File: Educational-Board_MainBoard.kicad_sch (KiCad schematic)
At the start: 0 parts

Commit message: Aggiunto nomi
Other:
- company: (none) -> Filippo Castellan, Alan Masutti
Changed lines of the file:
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@@
 	(generator_version "9.0")
 	(paper "A4")
+	(title_block
+		(date "2025-09-29")
+		(company "Filippo Castellan, Alan Masutti")
+	)
 	(sheet_instances
 		(path "/"

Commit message: Aggiunto schema generale alimentazione e UI. Da fare sourcing componenti
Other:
- added sheet Power (Power.kicad_sch)
- added sheet UI (UI.kicad_sch)
- title: (none) -> Think Embedded dev Board
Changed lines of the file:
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@@
 	(paper "A4")
 	(title_block
-		(date "2025-09-29")
+		(title "Think Embedded dev Board")
+		(date "2026-01-11")
+		(rev "1.0")
 		(company "Filippo Castellan, Alan Masutti")
 	)
+	(sheet
+		(at 186.69 90.17)
+		(size 24.13 25.4)
+		(exclude_from_sim no)
+		(in_bom yes)
+		(on_board yes)
+		(dnp no)
+		(fields_autoplaced yes)
+		(stroke
+			(width 0.1524)
+			(type solid)
+		)
+		(fill
+			(color 0 0 0 0.0000)
+		)
+		(property "Sheetname" "UI"
+			(at 186.69 89.4584 0)
+			(effects
+				(font
+					(size 1.27 1.27)
+				)
+				(justify left bottom)
+			)
+		)
+		(property "Sheetfile" "UI.kicad_sch"
+			(at 186.69 116.1546 0)
+			(effects
+				(font
+					(size 1.27 1.27)
+				)
+				(justify left top)
+				(hide yes)
+			)
+		)
+		(instances
+			(project "Educational-Board_MainBoard"
+				(path "/835b4df9-7d62-45f4-81d2-5a64fbc86f3c"
+					(page "3")
+				)
+			)
+		)
+	)
+	(sheet
+		(at 59.69 92.71)
+		(size 22.86 22.86)
+		(exclude_from_sim no)
+		(in_bom yes)
+		(on_board yes)
+		(dnp no)
+		(fields_autoplaced yes)
+		(stroke
+			(width 0.1524)
+			(type solid)
+		)
+		(fill
+			(color 0 0 0 0.0000)
+		)
+		(property "Sheetname" "Power"
+			(at 59.69 91.9984 0)
+			(effects
+				(font
+					(size 1.27 1.27)
+				)
+				(justify left bottom)
+			)
+		)
+		(property "Sheetfile" "Power.kicad_sch"
+			(at 59.69 116.1546 0)
+			(effects
+				(font
+					(size 1.27 1.27)
+				)
+				(justify left top)
+				(hide yes)
+			)
+		)
+		(pin "NUCLEO_5V" input
+			(at 82.55 105.41 0)
+			(effects
+				(font
+					(size 1.27 1.27)
+				)
+				(justify right)
+			)
+		)
+		(instances
+			(project "Educational-Board_MainBoard"
+				(path "/835b4df9-7d62-45f4-81d2-5a64fbc86f3c"
+					(page "2")
+				)
+			)
+		)
+	)
 	(sheet_instances

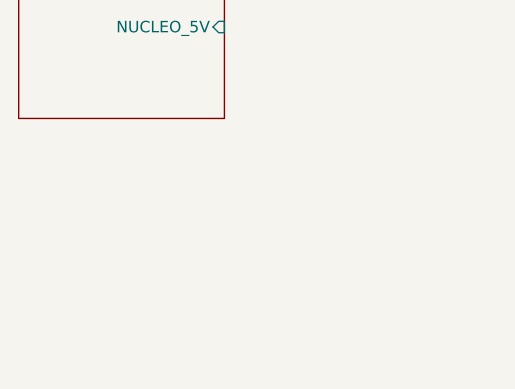
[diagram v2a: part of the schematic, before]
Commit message: Sistemato disaccoppiamento pulasnti, e aggiunto gyro i2c
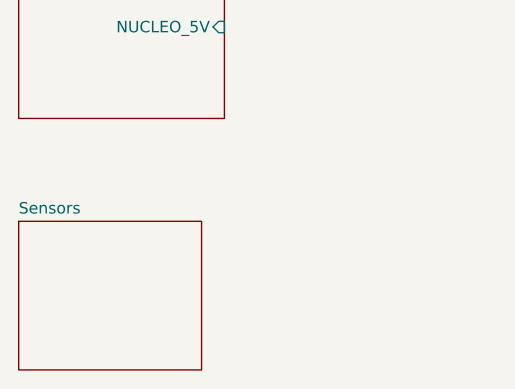
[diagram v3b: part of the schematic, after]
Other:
- added sheet Sensors (sensors.kicad_sch)
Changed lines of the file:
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@@
+		)
+	)
+	(sheet
+		(at 59.69 127)
+		(size 20.32 16.51)
+		(exclude_from_sim no)
+		(in_bom yes)
+		(on_board yes)
+		(dnp no)
+		(fields_autoplaced yes)
+		(stroke
+			(width 0.1524)
+			(type solid)
+		)
+		(fill
+			(color 0 0 0 0.0000)
+		)
+		(property "Sheetname" "Sensors"
+			(at 59.69 126.2884 0)
+			(effects
+				(font
+					(size 1.27 1.27)
+				)
+				(justify left bottom)
+			)
+		)
+		(property "Sheetfile" "sensors.kicad_sch"
+			(at 59.69 144.0946 0)
+			(effects
+				(font
+					(size 1.27 1.27)
+				)
+				(justify left top)
+				(hide yes)
+			)
+		)
+		(instances
+			(project "Educational-Board_MainBoard"
+				(path "/835b4df9-7d62-45f4-81d2-5a64fbc86f3c"
+					(page "4")
+				)
+			)
 		)
 	)

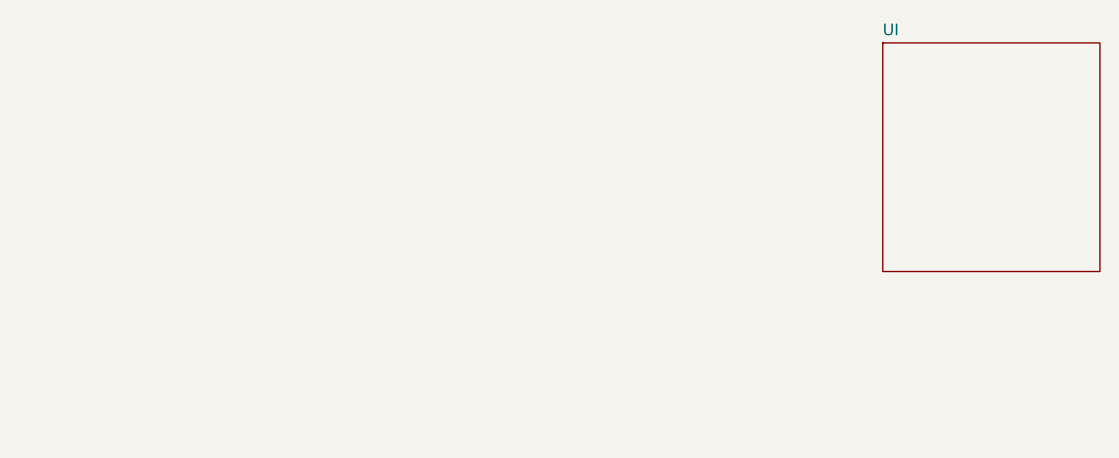
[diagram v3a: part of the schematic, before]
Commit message: Added MCU sheet + added a button on the UI sheet
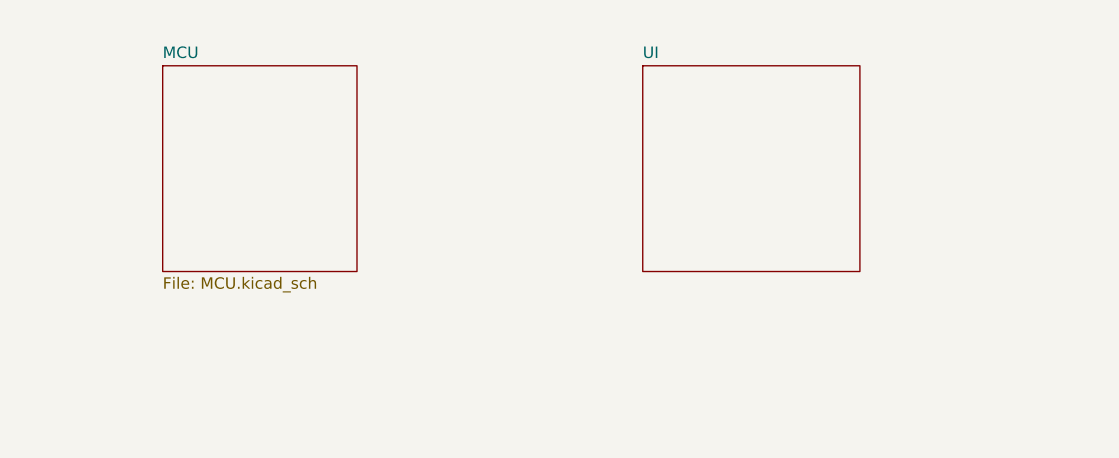
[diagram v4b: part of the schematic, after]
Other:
- added sheet MCU (MCU.kicad_sch)
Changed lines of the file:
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@@
 	)
 	(sheet
-		(at 186.69 90.17)
-		(size 24.13 25.4)
+		(at 160.02 92.71)
+		(size 24.13 22.86)
 		(exclude_from_sim no)
 		(in_bom yes)
@@
 		)
 		(property "Sheetname" "UI"
-			(at 186.69 89.4584 0)
+			(at 160.02 91.9984 0)
 			(effects
 				(font
@@
 		)
 		(property "Sheetfile" "UI.kicad_sch"
-			(at 186.69 116.1546 0)
+			(at 160.02 116.1546 0)
 			(effects
 				(font
@@
 				)
 			)
+		)
+	)
+	(sheet
+		(at 106.68 92.71)
+		(size 21.59 22.86)
+		(exclude_from_sim no)
+		(in_bom yes)
+		(on_board yes)
+		(dnp no)
+		(fields_autoplaced yes)
+		(stroke
+			(width 0.1524)
+			(type solid)
+		)
+		(fill
+			(color 0 0 0 0.0000)
+		)
+		(property "Sheetname" "MCU"
+			(at 106.68 91.9984 0)
+			(effects
+				(font
+					(size 1.27 1.27)
+				)
+				(justify left bottom)
+			)
+		)
+		(property "Sheetfile" "MCU.kicad_sch"
+			(at 106.68 116.1546 0)
+			(effects
+				(font
+					(size 1.27 1.27)
+				)
+				(justify left top)
+			)
+		)
+		(instances
+			(project "Educational-Board_MainBoard"
+				(path "/835b4df9-7d62-45f4-81d2-5a64fbc86f3c"
+					(page "5")
+				)
+			)

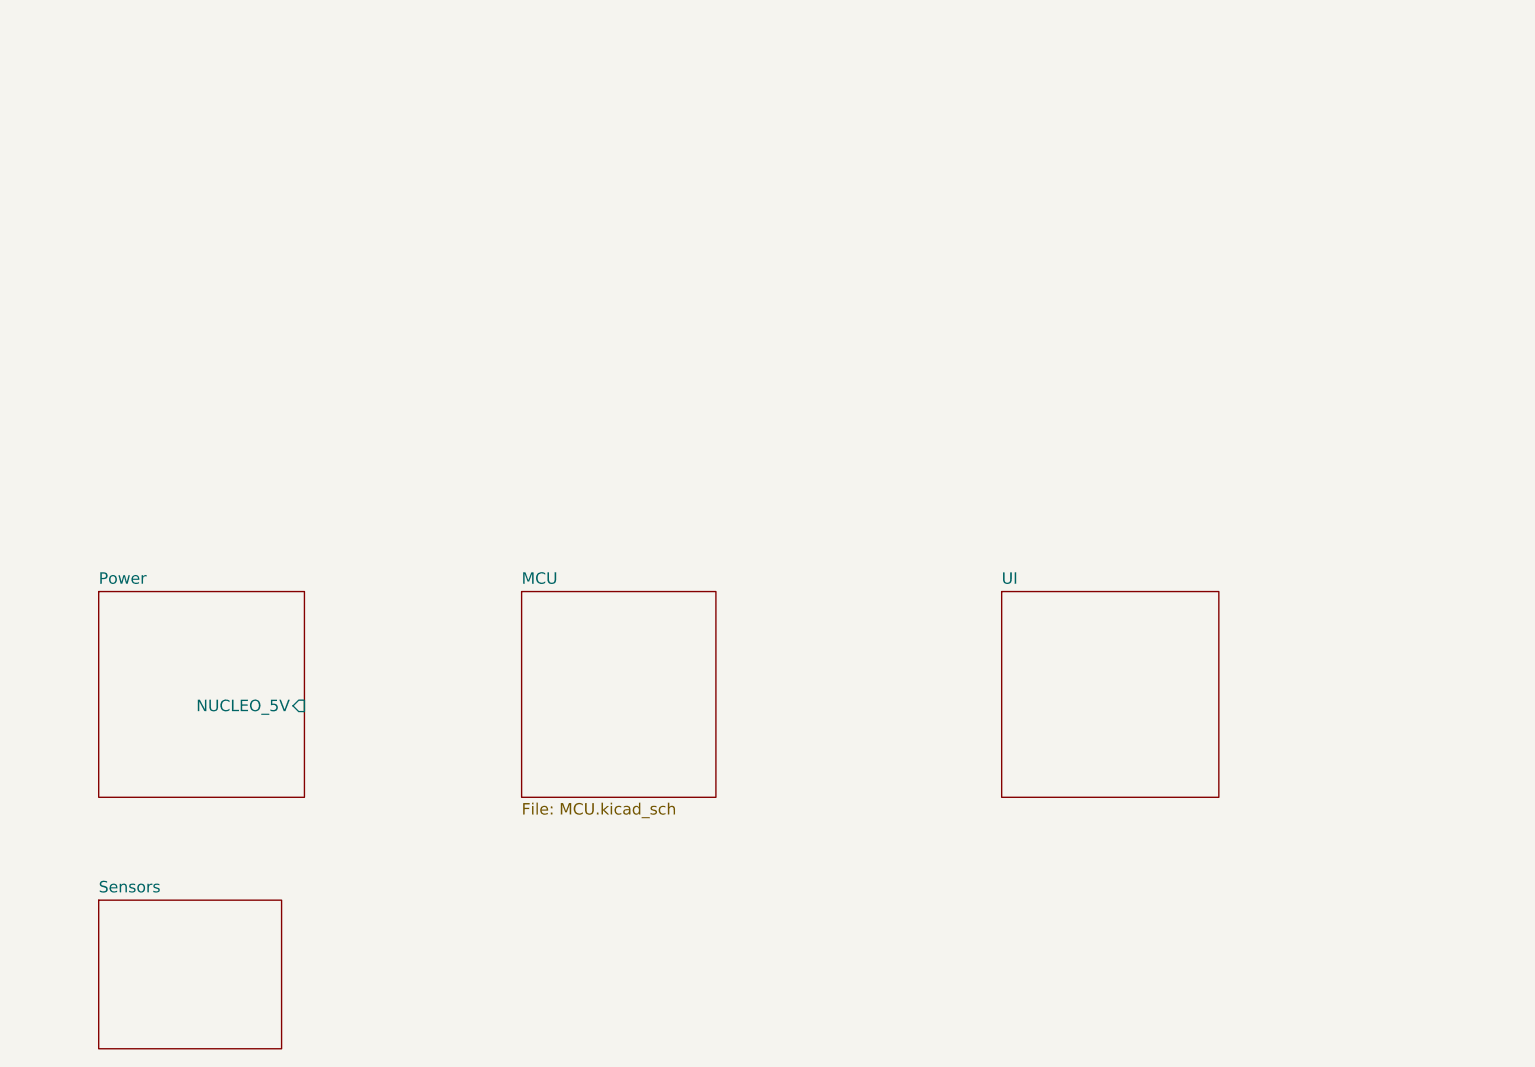
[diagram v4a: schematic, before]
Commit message: Connected the nucleo to local nets
 - I created all the local lables to the MCU schematic and connected them to the corresponding pins of the Nucleo board.
 - I renumed the hierarchical sheets to be in order of importance
 - I added solder jumpers for making the board more versatile in some cases
 - Corrected the Nucleo pinout on the schematic symbol
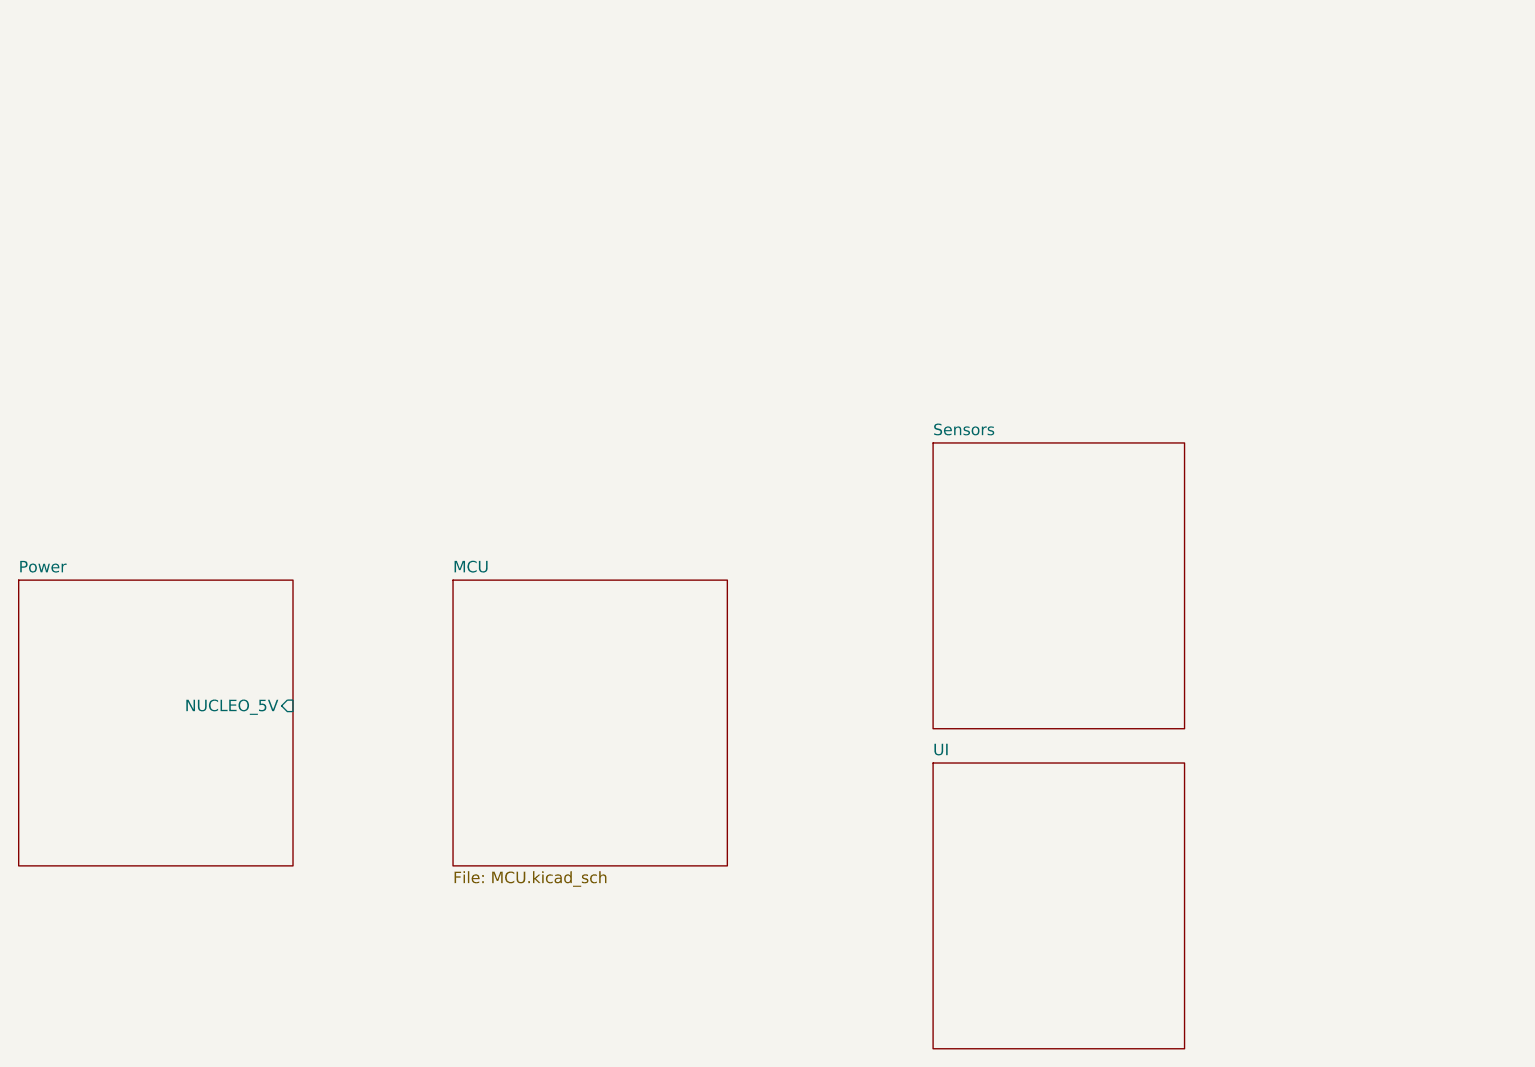
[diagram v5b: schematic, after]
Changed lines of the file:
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@@
 	)
 	(sheet
-		(at 160.02 92.71)
-		(size 24.13 22.86)
+		(at 152.4 111.76)
+		(size 27.94 31.75)
 		(exclude_from_sim no)
 		(in_bom yes)
@@
 		)
 		(property "Sheetname" "UI"
-			(at 160.02 91.9984 0)
+			(at 152.4 111.0484 0)
 			(effects
 				(font
@@
 		)
 		(property "Sheetfile" "UI.kicad_sch"
-			(at 160.02 116.1546 0)
+			(at 152.4 144.0946 0)
 			(effects
 				(font
@@
 			(project "Educational-Board_MainBoard"
 				(path "/835b4df9-7d62-45f4-81d2-5a64fbc86f3c"
-					(page "3")
+					(page "5")
 				)
 			)
@@
 	)
 	(sheet
-		(at 59.69 92.71)
-		(size 22.86 22.86)
+		(at 50.8 91.44)
+		(size 30.48 31.75)
 		(exclude_from_sim no)
 		(in_bom yes)
@@
 		)
 		(property "Sheetname" "Power"
-			(at 59.69 91.9984 0)
+			(at 50.8 90.7284 0)
 			(effects
 				(font
@@
 		)
 		(property "Sheetfile" "Power.kicad_sch"
-			(at 59.69 116.1546 0)
+			(at 50.8 123.7746 0)
 			(effects
 				(font
@@
 		)
 		(pin "NUCLEO_5V" input
-			(at 82.55 105.41 0)
+			(at 81.28 105.41 0)
 			(effects
 				(font
@@
 	)
 	(sheet
-		(at 106.68 92.71)
-		(size 21.59 22.86)
+		(at 99.06 91.44)
+		(size 30.48 31.75)
 		(exclude_from_sim no)
 		(in_bom yes)
@@
 		)
 		(property "Sheetname" "MCU"
-			(at 106.68 91.9984 0)
+			(at 99.06 90.7284 0)
 			(effects
 				(font
@@
 		)
 		(property "Sheetfile" "MCU.kicad_sch"
-			(at 106.68 116.1546 0)
+			(at 99.06 123.7746 0)
 			(effects
 				(font
@@
 			(project "Educational-Board_MainBoard"
 				(path "/835b4df9-7d62-45f4-81d2-5a64fbc86f3c"
-					(page "5")
+					(page "3")
 				)
 			)
@@
 	)
 	(sheet
-		(at 59.69 127)
-		(size 20.32 16.51)
+		(at 152.4 76.2)
+		(size 27.94 31.75)
 		(exclude_from_sim no)
 		(in_bom yes)
@@
 		)
 		(property "Sheetname" "Sensors"
-			(at 59.69 126.2884 0)
+			(at 152.4 75.4884 0)
 			(effects
 				(font
@@
 		)
 		(property "Sheetfile" "sensors.kicad_sch"
-			(at 59.69 144.0946 0)
+			(at 152.4 108.5346 0)
 			(effects
 				(font

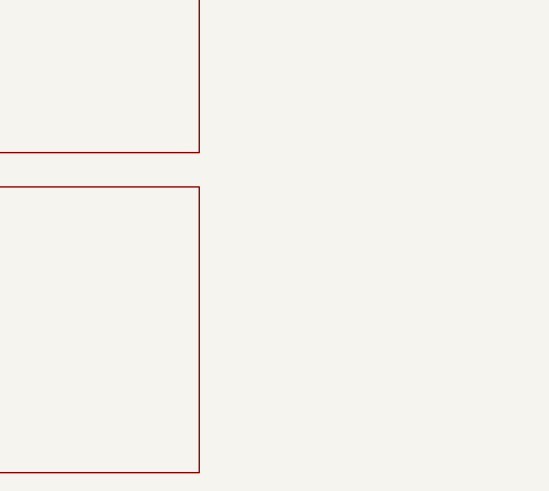
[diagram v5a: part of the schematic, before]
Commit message: Added BME280 on Sensor sheet + Added Power frontend on the dedicated sheet + added I2C Resistors + minor changes
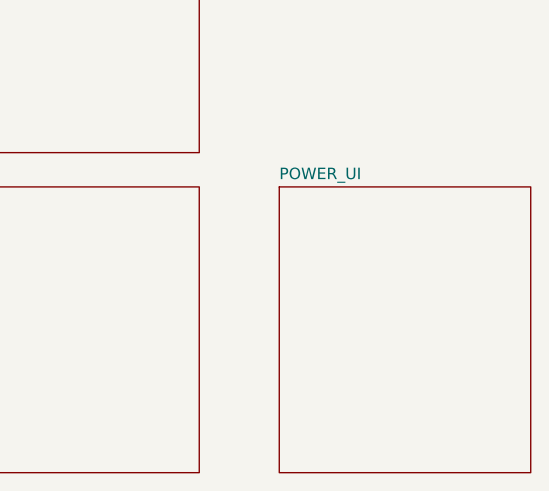
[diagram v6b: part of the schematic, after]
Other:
- added sheet POWER_UI (POWER_UI.kicad_sch)
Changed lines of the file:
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@@
+	)
+	(sheet
+		(at 189.23 111.76)
+		(size 27.94 31.75)
+		(exclude_from_sim no)
+		(in_bom yes)
+		(on_board yes)
+		(dnp no)
+		(fields_autoplaced yes)
+		(stroke
+			(width 0.1524)
+			(type solid)
+		)
+		(fill
+			(color 0 0 0 0.0000)
+		)
+		(property "Sheetname" "POWER_UI"
+			(at 189.23 111.0484 0)
+			(effects
+				(font
+					(size 1.27 1.27)
+				)
+				(justify left bottom)
+			)
+		)
+		(property "Sheetfile" "POWER_UI.kicad_sch"
+			(at 189.23 144.0946 0)
+			(effects
+				(font
+					(size 1.27 1.27)
+				)
+				(justify left top)
+				(hide yes)
+			)
+		)
+		(instances
+			(project "Educational-Board_MainBoard"
+				(path "/835b4df9-7d62-45f4-81d2-5a64fbc86f3c"
+					(page "6")
+				)
+			)
+		)
 	)
 	(sheet
